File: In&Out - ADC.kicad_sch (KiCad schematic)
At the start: 0 parts

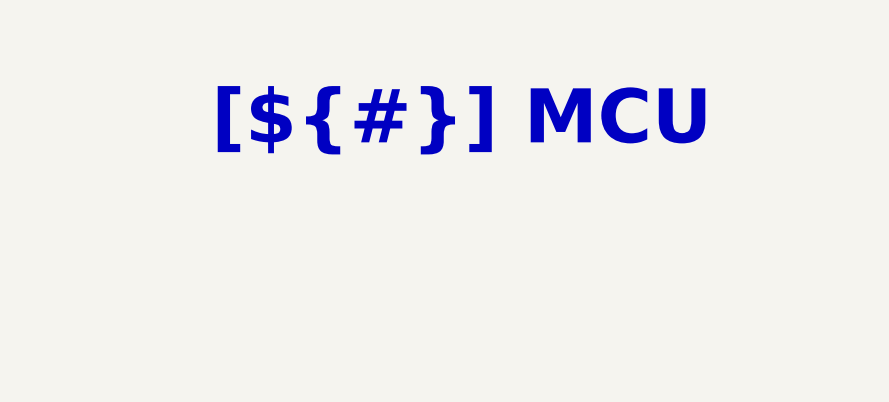
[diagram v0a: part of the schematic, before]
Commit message: [Project][Added] CI/CD environment
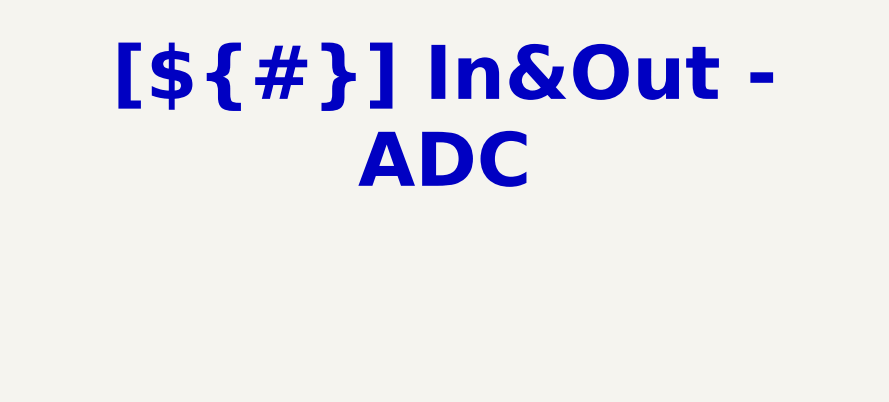
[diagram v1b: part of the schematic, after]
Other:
- title: MCU -> In&Out - ADC
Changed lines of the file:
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@@
 	(paper "A4")
 	(title_block
-		(title "MCU")
+		(title "In&Out - ADC")
 		(date "2025-01-12")
 		(rev "${REVISION}")
@@
 	(text_box "[${#}] ${TITLE}"
 		(exclude_from_sim no)
-		(at 115.57 15.24 0)
-		(size 72.39 12.7)
+		(at 100.33 15.24 0)
+		(size 99.06 12.7)
 		(margins 4.4999 4.4999 4.4999 4.4999)
 		(stroke

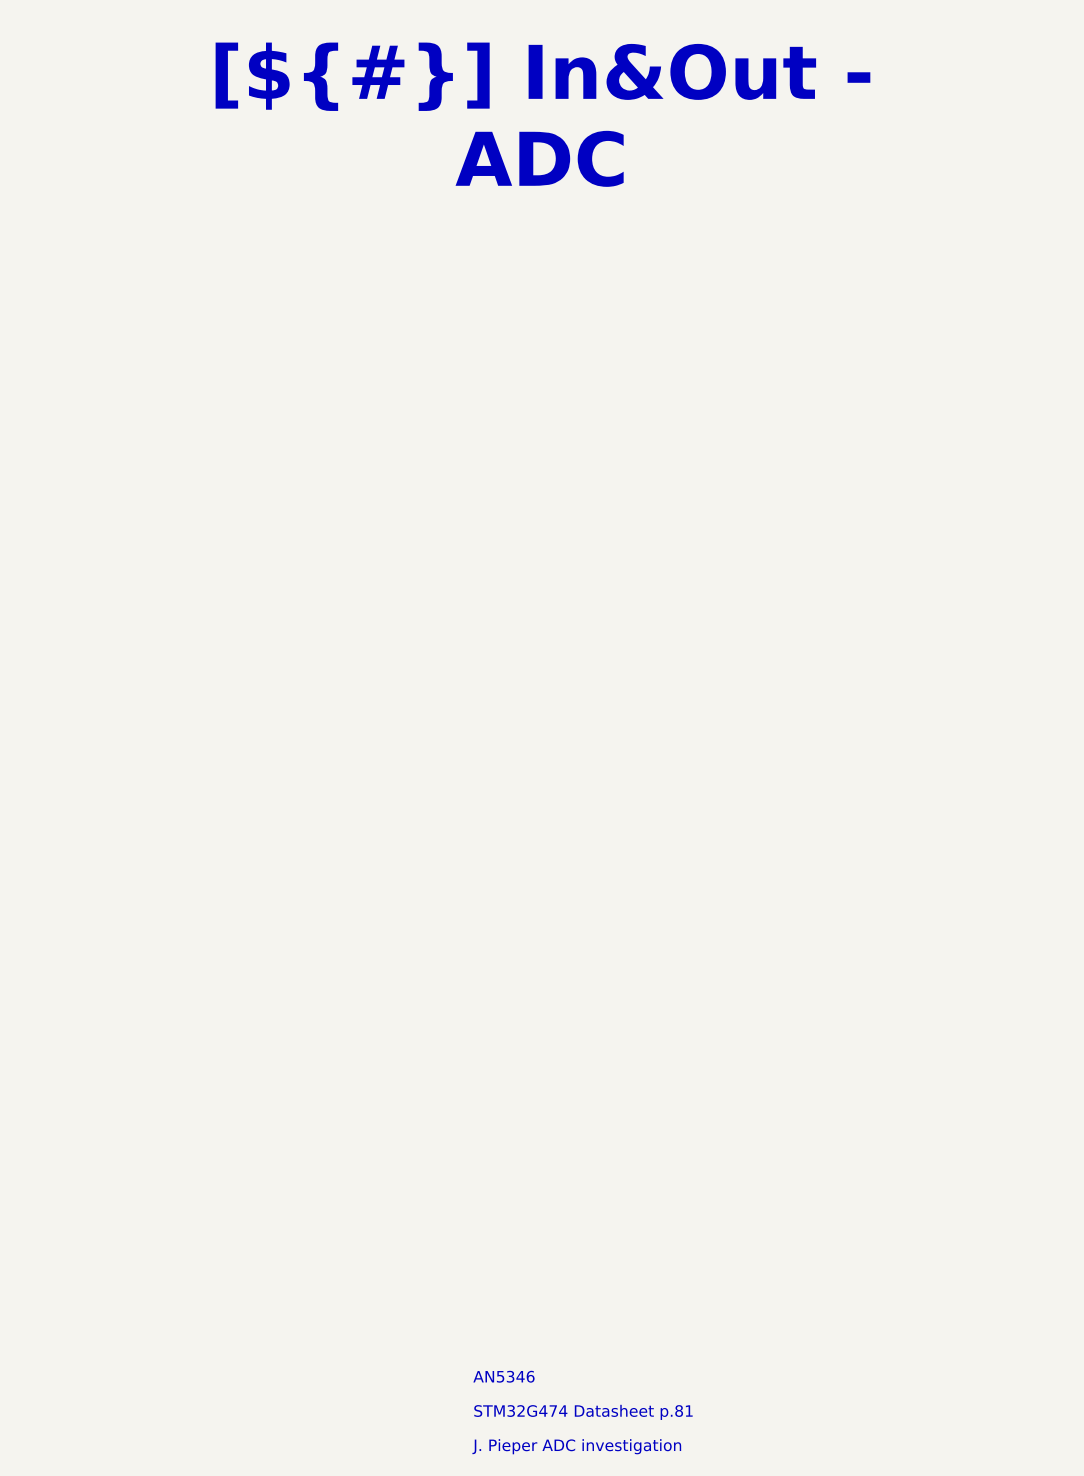
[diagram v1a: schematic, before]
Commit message: [Project][Added] CI/CD environment
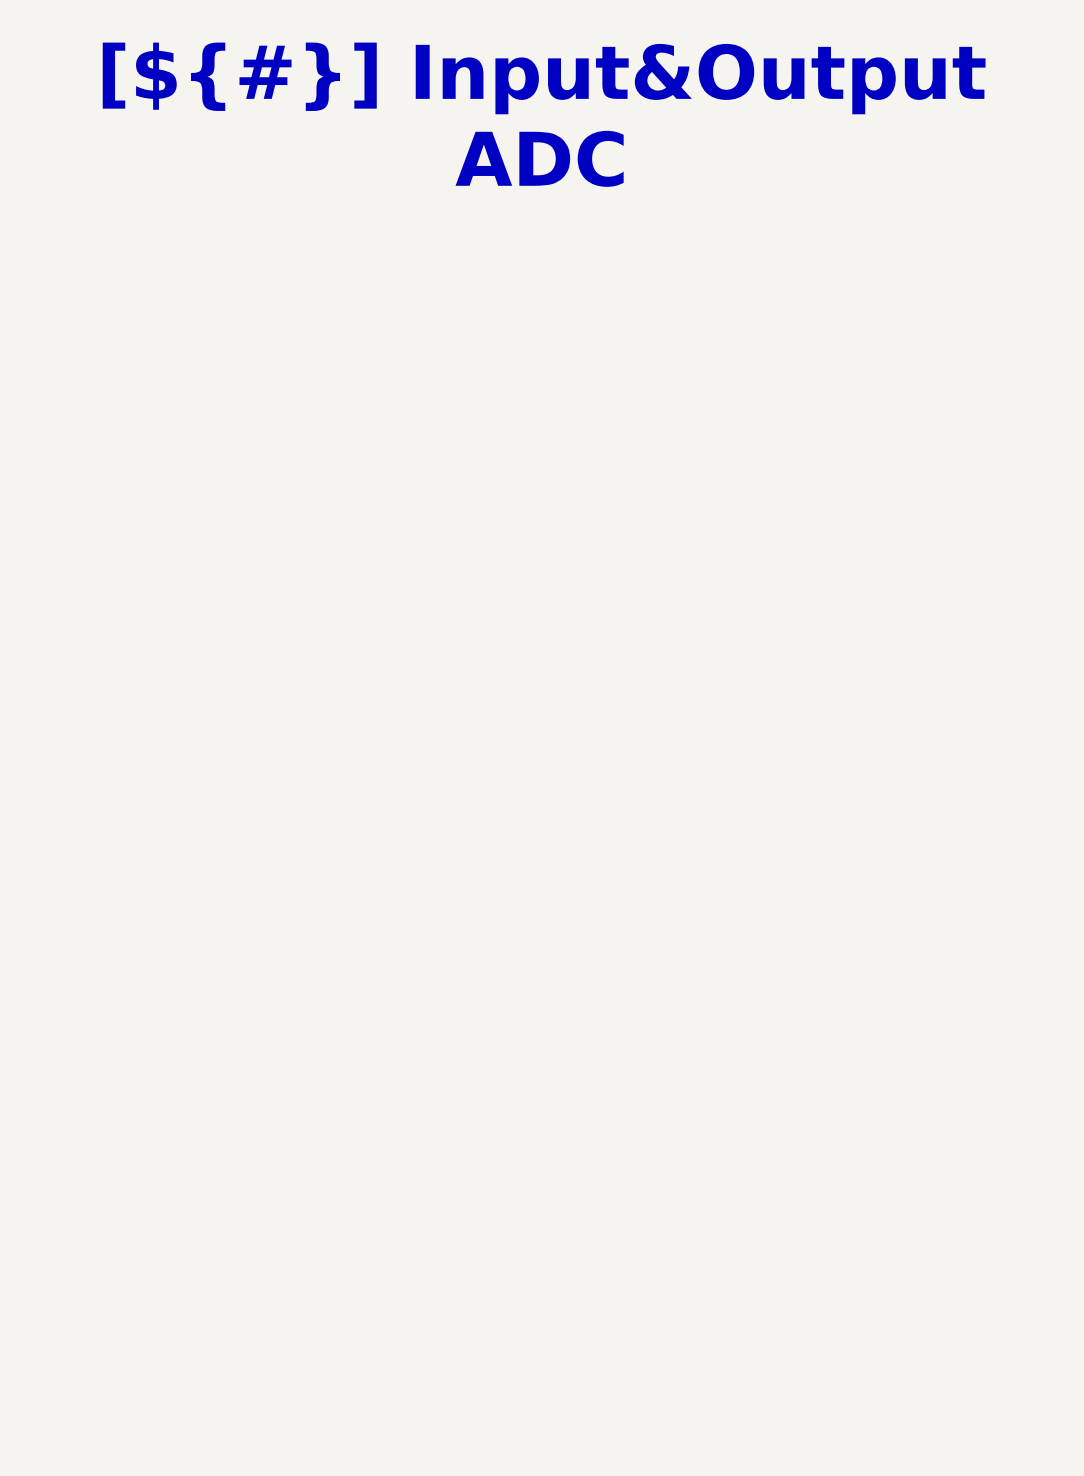
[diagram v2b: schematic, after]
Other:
- note removed: "AN5346"
- note removed: "J. Pieper ADC investigation"
- note removed: "STM32G474 Datasheet p.81"
- title: In&Out - ADC -> Input&Output ADC
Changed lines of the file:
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@@
 (kicad_sch
-	(version 20260306)
+	(version 20250114)
 	(generator "eeschema")
-	(generator_version "10.0")
+	(generator_version "9.0")
 	(paper "A4")
 	(title_block
-		(title "In&Out - ADC")
+		(title "Input&Output ADC")
 		(date "2025-01-12")
 		(rev "${REVISION}")
 		(company "${COMPANY}")
 	)
-	(text "J. Pieper ADC investigation"
-		(exclude_from_sim no)
-		(at 142.24 170.18 0)
-		(effects
-			(font
-				(face "Arial")
-				(size 1.27 1.27)
-				(color 0 0 0 1)
-			)
-			(justify left bottom)
-			(href "https://jpieper.com/2023/07/24/stm32g4-adc-performance-part-2/")
-		)
-	)
-	(text "STM32G474 Datasheet p.81"
-		(exclude_from_sim no)
-		(at 142.24 166.37 0)
-		(effects
-			(font
-				(face "Arial")
-				(size 1.27 1.27)
-				(color 0 0 0 1)
-			)
-			(justify left bottom)
-			(href "https://www.st.com/resource/en/datasheet/stm32g474cb.pdf")
-		)
-	)
-	(text "AN5346"
-		(exclude_from_sim no)
-		(at 142.24 162.56 0)
-		(effects
-			(font
-				(face "Arial")
-				(size 1.27 1.27)
-				(color 0 0 0 1)
-			)
-			(justify left bottom)
-			(href "https://www.st.com/resource/en/application_note/an5346-stm32g4-adc-use-tips-and-recommendations-stmicroelectronics.pdf")
-		)
-	)
 	(text_box "[${#}] ${TITLE}"
 		(exclude_from_sim no)
-		(at 100.33 15.24 0)
-		(size 99.06 12.7)
+		(at 95.25 15.24 0)
+		(size 109.22 12.7)
 		(margins 4.4999 4.4999 4.4999 4.4999)
 		(stroke

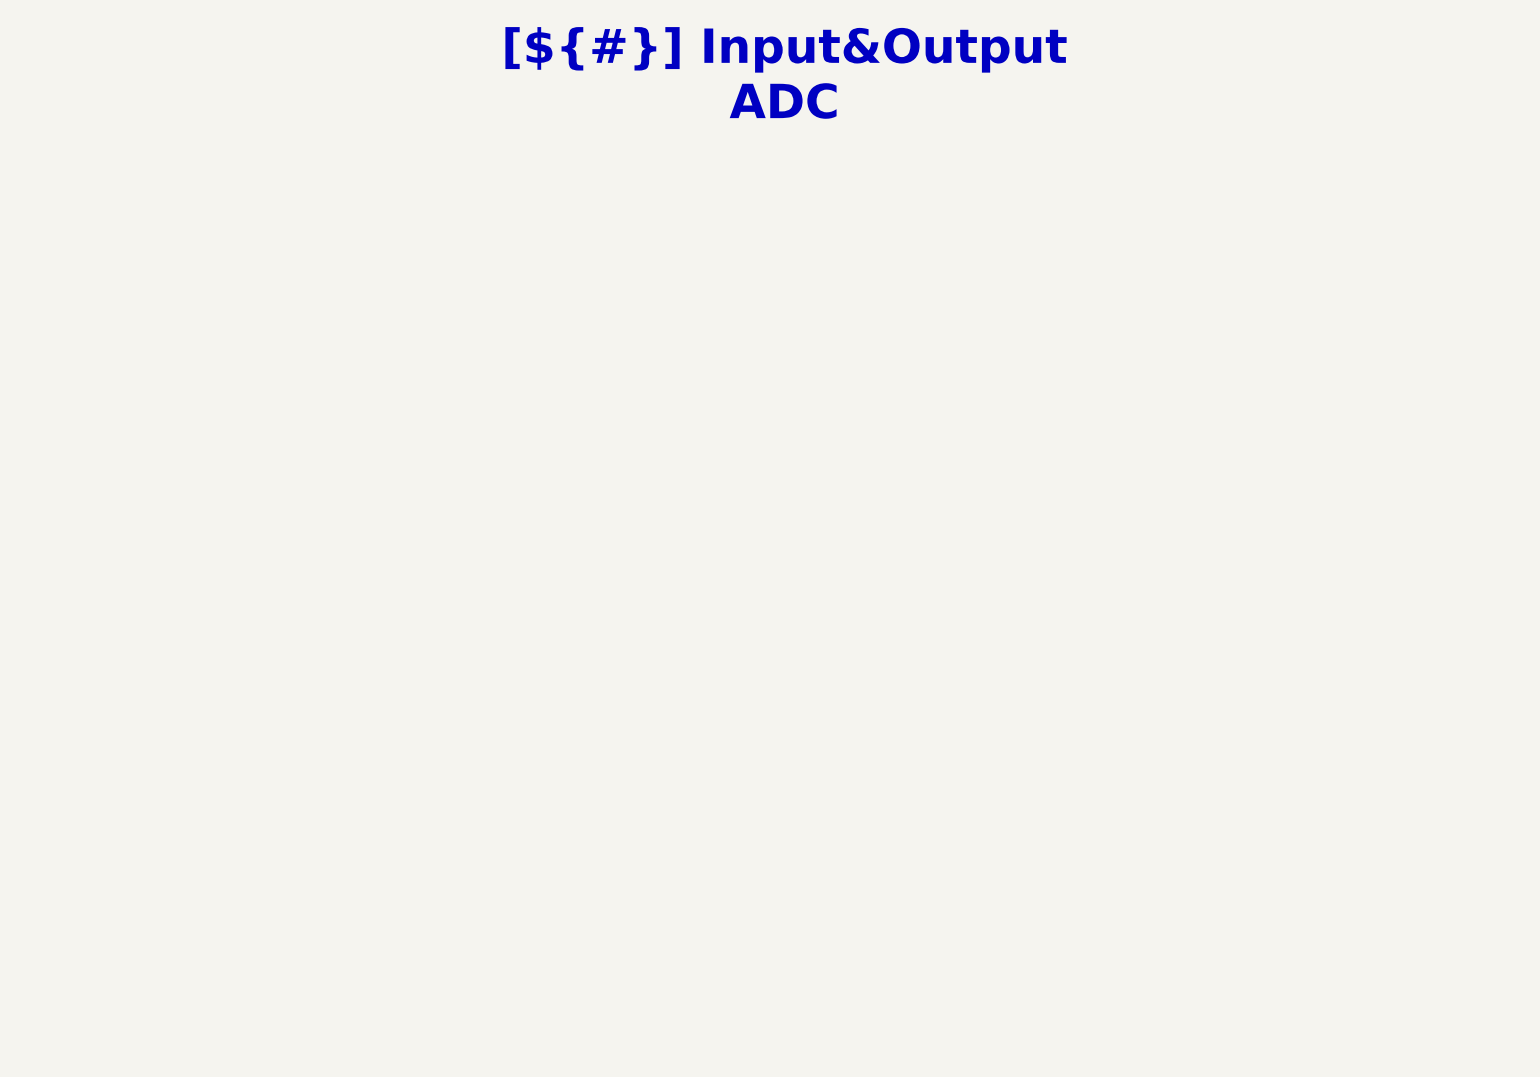
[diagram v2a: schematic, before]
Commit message: [Schematic][Add] In&Out - ADC, add schematic
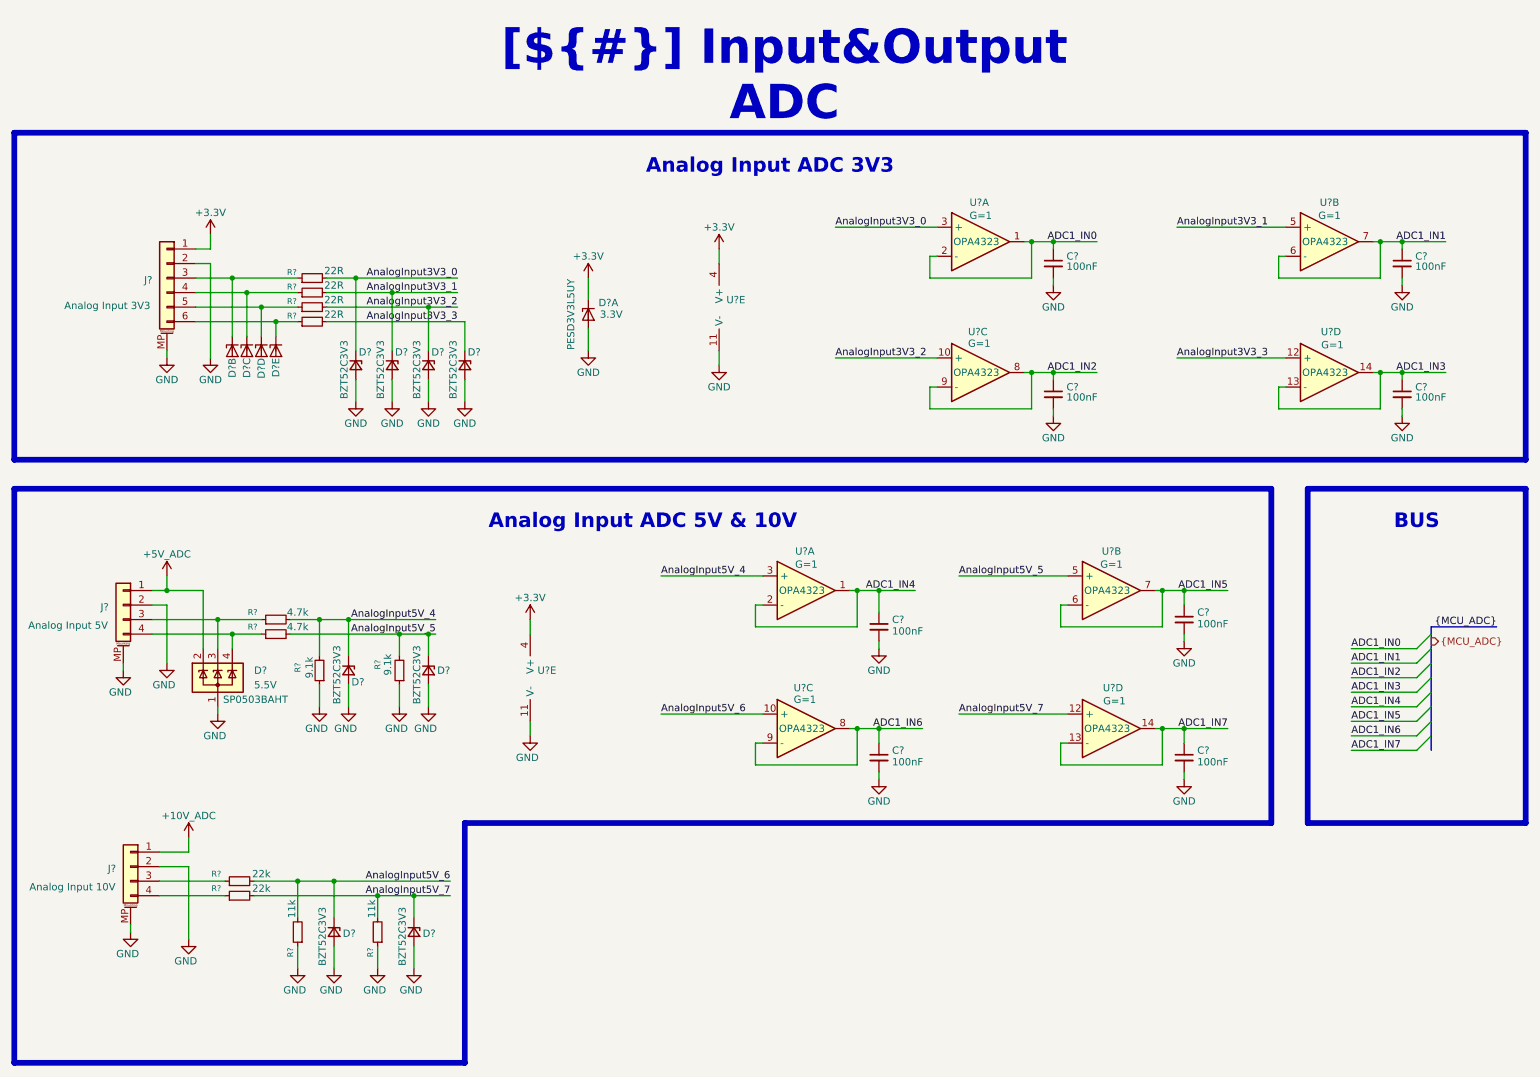
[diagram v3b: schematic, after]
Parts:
- added C? (x8): 100nF, Capacitor_SMD:C_0603_1608Metric_Pad1.08x0.95mm_HandSolder, symbol Device:C_Small
- added D? (x5): 3.3V, Package_TO_SOT_SMD:SOT-363_SC-70-6, symbol Power_Protection:PESD3V3L5UY
- added D? (x8): 3.3V, Diode_SMD:D_SOD-123F, symbol Device:D_Zener_Small
- added D?: 5.5V, Package_TO_SOT_SMD:SOT-143, symbol Power_Protection:SP0503BAHT
- added J? (x2): *, Connector_JST:JST_PH_S4B-PH-SM4-TB_1x04-1MP_P2.00mm_Horizontal, symbol Connector_Generic_MountingPin:Conn_01x04_MountingPin
- added J?: *, Connector_JST:JST_PH_S6B-PH-SM4-TB_1x06-1MP_P2.00mm_Horizontal, symbol Connector_Generic_MountingPin:Conn_01x06_MountingPin
- added R? (x2): 11k, Resistor_SMD:R_0805_2012Metric_Pad1.20x1.40mm_HandSolder, symbol Device:R_Small
- added R? (x4): 22R, Resistor_SMD:R_0805_2012Metric_Pad1.20x1.40mm_HandSolder, symbol Device:R_Small
- added R? (x2): 9.1k, Resistor_SMD:R_0805_2012Metric_Pad1.20x1.40mm_HandSolder, symbol Device:R_Small
- added R? (x2): 22k, Resistor_SMD:R_0805_2012Metric_Pad1.20x1.40mm_HandSolder, symbol Device:R_Small
- added R? (x2): 4.7k, Resistor_SMD:R_0805_2012Metric_Pad1.20x1.40mm_HandSolder, symbol Device:R_Small
- added U? (x10): G=1, Package_SO:TSSOP-14_4.4x5mm_P0.65mm, symbol Amplifier_Operational:Opamp_Quad
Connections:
- new net: D?.4 (K3), J?.4 (Pin_4), R?.1
- new net: J?.3 (Pin_3), R?.1
- new net: J?.4 (Pin_4), R?.1
- new net: D?.3 (K2), J?.3 (Pin_3), R?.1
- new net: D?.5 (K4), J?.5 (Pin_5), R?.1
- new net: D?.6 (K5), J?.6 (Pin_6), R?.1
- new net: D?.3 (K), J?.3 (Pin_3), R?.1
- new net: D?.4 (K), J?.4 (Pin_4), R?.1
- new net +10V_ADC: J?.1 (Pin_1)
- new net +3.3V: D?.1 (K1), J?.1 (Pin_1), U?.4 (V+), U?.4 (V+)
- new net +5V_ADC: D?.2 (K), J?.1 (Pin_1)
- new net ADC1_IN0: C?.1, U?.1, U?.2 (-)
- new net ADC1_IN1: C?.1, U?.6 (-), U?.7
- new net ADC1_IN2: C?.1, U?.8, U?.9 (-)
- new net ADC1_IN3: C?.1, U?.13 (-), U?.14
- new net ADC1_IN4: C?.1, U?.1, U?.2 (-)
- new net ADC1_IN5: C?.1, U?.6 (-), U?.7
- new net ADC1_IN6: C?.1, U?.8, U?.9 (-)
- new net ADC1_IN7: C?.1, U?.13 (-), U?.14
- new net AnalogInput3V3_0: D?.1 (K), R?.2, U?.3 (+)
- new net AnalogInput3V3_1: D?.1 (K), R?.2, U?.5 (+)
- new net AnalogInput3V3_2: D?.1 (K), R?.2, U?.10 (+)
- new net AnalogInput3V3_3: D?.1 (K), R?.2, U?.12 (+)
- new net AnalogInput5V_4: D?.1 (K), R?.2, R?.2, U?.3 (+)
- new net AnalogInput5V_5: D?.1 (K), R?.2, R?.2, U?.5 (+)
- new net AnalogInput5V_6: D?.1 (K), R?.2, R?.2, U?.10 (+)
- new net AnalogInput5V_7: D?.1 (K), R?.2, R?.2, U?.12 (+)
- new net GND: C?.2, C?.2, C?.2, C?.2, C?.2, C?.2, C?.2, C?.2, D?.1 (A), D?.2 (A), D?.2 (A), D?.2 (A), D?.2 (A), D?.2 (A), D?.2 (A), D?.2 (A), D?.2 (A), D?.2 (A), J?.2 (Pin_2), J?.2 (Pin_2), J?.2 (Pin_2), J?.MP (MountPin), J?.MP (MountPin), J?.MP (MountPin), R?.1, R?.1, R?.1, R?.1, U?.11 (V-), U?.11 (V-)
